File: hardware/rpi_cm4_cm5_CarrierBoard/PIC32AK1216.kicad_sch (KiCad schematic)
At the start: 96 parts, among them J10 PR20206VBNN, Q21 2N7002, Q25 2N7002, Q26 2N7002, U1 PIC32AK1216GC41064-I/M7, U20 STWD100NYWY3F, Y3 20MHz

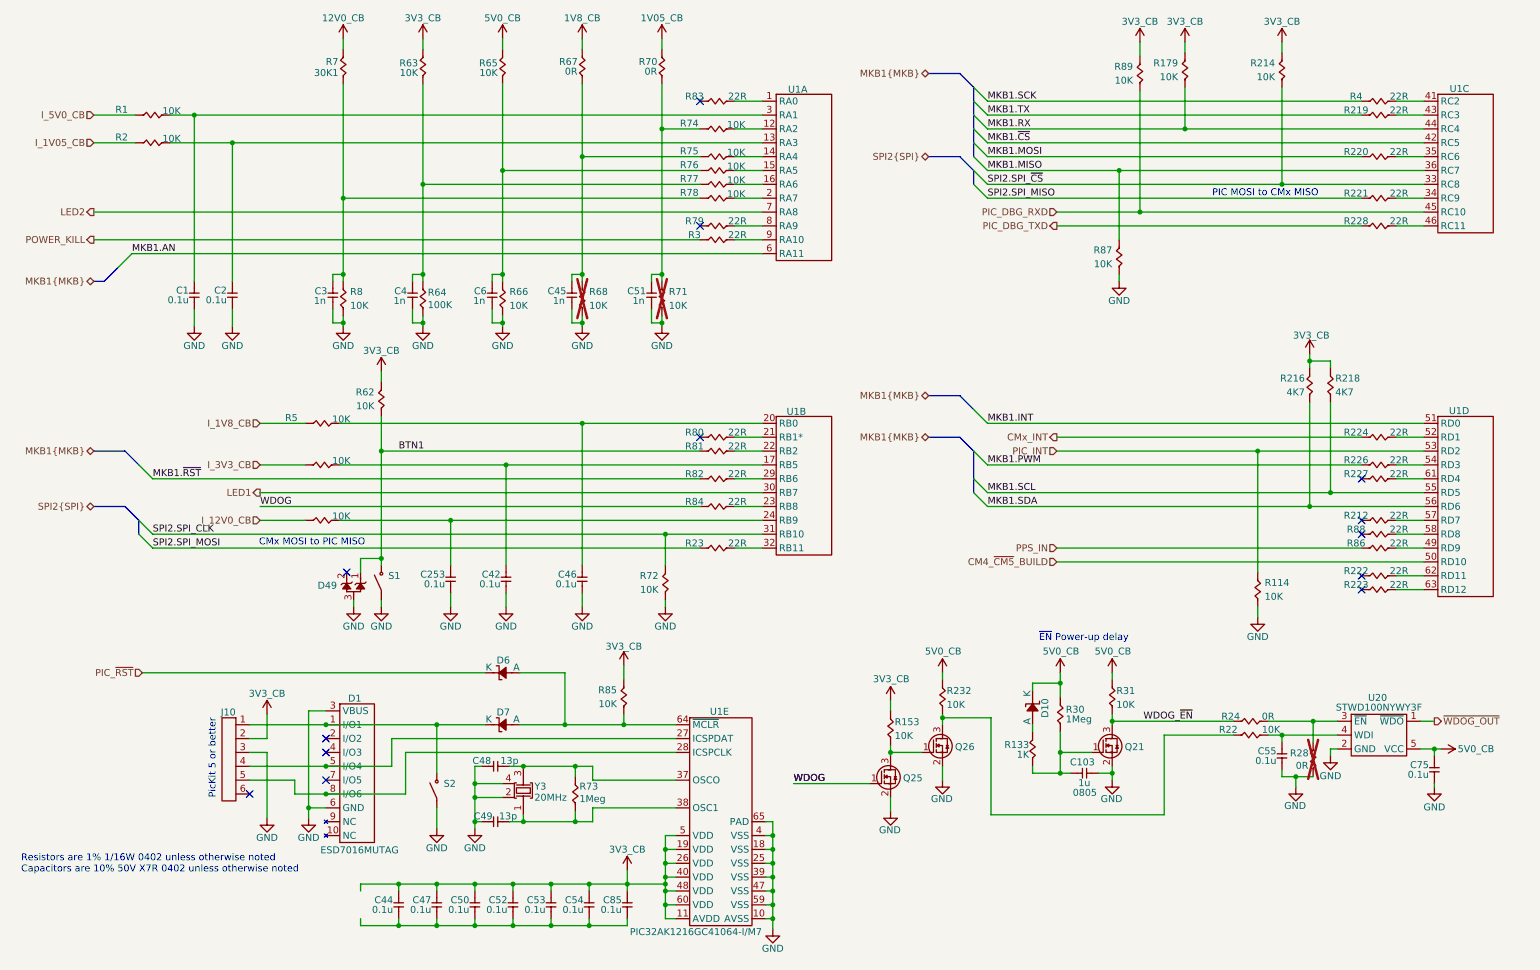
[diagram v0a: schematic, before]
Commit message: Cosmetic adjustments to schematics
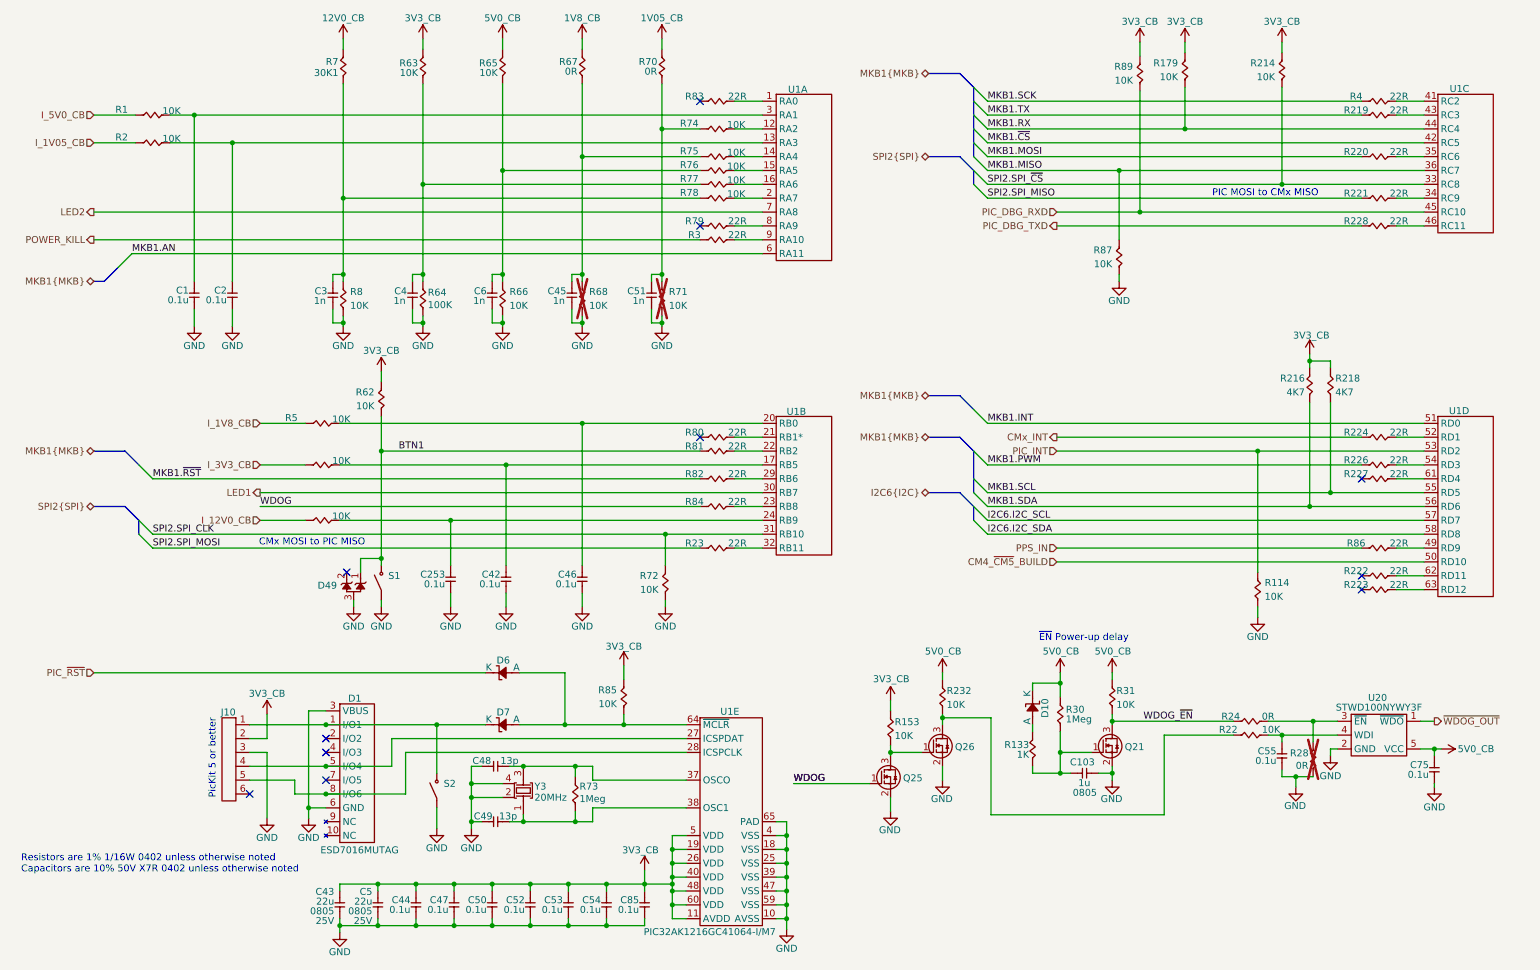
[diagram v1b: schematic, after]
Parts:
- removed R212, R88: 22R, footprint:RES_0402, symbol KicadCompDb:Resistors/RES_SMT_00015
- added C43, C5: 22u, footprint:CAP_NONPOL_0805, symbol KicadCompDb:Capacitors/CAP_CER_SMT_00011
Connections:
- net 3V3_CB: now also C43.2, C5.2
- net GND: now also C44.1, C47.1, C50.1, C52.1, C53.1, C54.1, C85.1, C43.1, C5.1
- net I2C6.I2C_SCL: now reaches U1.57 (RD7)
- net I2C6.I2C_SDA: now reaches U1.58 (RD8)
- no-connect marks 13 -> 11
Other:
- moved on the sheet: C44, C47, C50, C52, C53, C54, C85, U1E

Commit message: Significant update in PCB layout; Completed preliminary high speed rules definition and fanout of differential pairs + GND vias. Started routing high speed signals Slight changes to Pinout based on component placement
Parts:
- removed R83: 22R, footprint:RES_0402, symbol KicadCompDb:Resistors/RES_SMT_00015
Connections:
- net LED2: now also U1.1 (RA0); no longer U1.7 (RA8)
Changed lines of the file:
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@@
 	)
 	(no_connect
-		(at 137.16 31.115)
-	)
-	(no_connect
 		(at 137.16 92.71)
 	)
@@
 		(at 137.16 53.975)
 	)
+	(no_connect
+		(at 148.59 51.435)
+	)
 	(bus_entry
 		(at 187.325 28.575)
@@
 	(wire
 		(pts
+			(xy 26.035 31.115) (xy 148.59 31.115)
+		)
+		(stroke
+			(width 0)
+			(type default)
+		)
+	)
+	(wire
+		(pts
 			(xy 198.12 154.305) (xy 203.2 154.305)
 		)
@@
 	(wire
 		(pts
-			(xy 26.035 51.435) (xy 148.59 51.435)
-		)
-		(stroke
-			(width 0)
-			(type default)
-		)
-	)
-	(wire
-		(pts
 			(xy 78.105 180.975) (xy 78.105 182.245)
 		)
@@
 	(wire
 		(pts
-			(xy 143.51 31.115) (xy 148.59 31.115)
-		)
-		(stroke
-			(width 0)
-			(type default)
-		)
-	)
-	(wire
-		(pts
 			(xy 51.435 38.735) (xy 148.59 38.735)
 		)
@@
 		)
 	)
+	(hierarchical_label "LED2"
+		(shape output)
+		(at 26.035 31.115 180)
+		(effects
+			(font
+				(size 1.27 1.27)
+			)
+			(justify right)
+		)
+	)
 	(hierarchical_label "~{WDOG_OUT}"
 		(shape output)
@@
 		)
 	)
-	(hierarchical_label "LED2"
-		(shape output)
-		(at 26.035 51.435 180)
-		(effects
-			(font
-				(size 1.27 1.27)
-			)
-			(justify right)
-		)
-	)
 	(hierarchical_label "I2C6{I2C}"
 		(shape bidirectional)
@@
 					(unit 1)
 				)
-			)
-		)
-	)
-	(symbol
-		(lib_id "KicadCompDb:Resistors/RES_SMT_00015")
-		(at 142.24 31.115 180)
-		(unit 1)
-		(exclude_from_sim no)
-		(in_bom yes)
-		(on_board yes)
-		(dnp no)
-		(property "Reference" "R83"
-			(at 136.144 30.226 0)
-			(effects
-				(font
-					(size 1.27 1.27)
-				)
-			)
-		)
-		(property "Value" "22R"
-			(at 144.018 30.226 0)
-			(effects
-				(font
-					(size 1.27 1.27)
-				)
-			)
-		)
-		(property "Footprint" "footprint:RES_0402"
-			(at 141.732 9.017 0)
-			(effects
-				(font
-					(size 1.27 1.27)
-				)
-				(hide yes)
-			)
-		)
-		(property "Datasheet" "https://www.yageogroup.com/content/datasheet/asset/file/PYU-RC_GROUP_51_ROHS_L"
-			(at 142.24 31.115 0)
-			(effects
-				(font
-					(size 1.27 1.27)
-				)
-				(hide yes)
-			)
-		)
-		(property "Description" "RES 22 OHM 1% 1/16W 0402"
-			(at 140.462 21.209 0)
-			(effects
-				(font
-					(size 1.27 1.27)
-				)
-				(hide yes)
-			)
-		)
-		(property "Tolerance" "1%"
-			(at 141.986 10.795 0)
-			(effects
-				(font
-					(size 1.27 1.27)
-				)
-				(hide yes)
-			)
-		)
-		(property "Power" "1/16W"
-			(at 141.986 16.891 0)
-			(effects
-				(font
-					(size 1.27 1.27)
-				)
-				(hide yes)
-			)
-		)
-		(property "Package" "0402"
-			(at 142.24 14.859 0)
-			(effects
-				(font
-					(size 1.27 1.27)
-				)
-				(hide yes)
-			)
-		)
-		(property "Manufacturer" "YAGEO"
-			(at 141.986 12.827 0)
-			(effects
-				(font
-					(size 1.27 1.27)
-				)
-				(hide yes)
-			)
-		)
-		(property "Manufacturer Part Number" "RC0402FR-0722RL"
-			(at 141.986 23.241 0)
-			(effects
-				(font
-					(size 1.27 1.27)
-				)
-				(hide yes)
-			)
-		)
-		(property "Distributor" "DigiKey"
-			(at 142.24 25.273 0)
-			(effects
-				(font
-					(size 1.27 1.27)
-				)
-				(hide yes)
-			)
-		)
-		(property "Distributor Part Number" "311-22.0LRCT-ND"
-			(at 141.478 18.923 0)
-			(effects
-				(font
-					(size 1.27 1.27)
-				)
-				(hide yes)
-			)
-		)
-		(property "Temperature Coefficient" "±100ppm/°C"
-			(at 142.24 31.115 0)
-			(effects
-				(font
-					(size 1.27 1.27)
-				)
-				(hide yes)
-			)
-		)
-		(property "Operating Temperature" "-55°C ~ 155°C"
-			(at 141.478 6.731 0)
-			(effects
-				(font
-					(size 1.27 1.27)
-				)
-				(hide yes)
-			)
-		)
-		(property "Type" "RES SMT"
-			(at 142.24 31.115 0)
-			(show_name yes)
-			(effects
-				(font
-					(size 1.27 1.27)
-				)
-				(hide yes)
-			)
-		)
-		(property "Dimensions" "1.00mm x 0.50mm"
-			(at 142.24 31.115 0)
-			(show_name yes)
-			(effects
-				(font
-					(size 1.27 1.27)
-				)
-				(hide yes)
-			)
-		)
-		(pin "1"
-		)
-		(pin "2"
-		)
-		(instances
-			(project "rpi_cm4_cm5_CarrierBoard"
-				(path "/7dcdf741-90ca-4333-848c-806f4d64158e/7cb911d0-d4f5-46a6-8f4b-d261141d8579"
-					(reference "R83")
-					(unit 1)
-				)

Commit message: Continue working on the layout. Completed most of power planes planning and pouring Completed all DiffPairs routing and length matching (preliminary)
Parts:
- removed C2: 0.1u, footprint:CAP_NONPOL_0402, symbol KicadCompDb:Capacitors/CAP_CER_SMT_00001
- removed R2: 10K, footprint:RES_0402, symbol KicadCompDb:Resistors/RES_SMT_00013
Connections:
- no-connect marks 11 -> 12

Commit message: Significant update Stackup changed from 6 to 8 layers Changed design notes accordingly Re-routed all differential pairs and length match / skew match Fanout critical signals away from dense areas 95% routing completed
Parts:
- removed R224: 22R, footprint:RES_0402, symbol KicadCompDb:Resistors/RES_SMT_00015
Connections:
- net CM4_~{CM5}_BUILD: now also U1.52 (RD1); no longer U1.50 (RD10)
- net CMx_INT: now also U1.50 (RD10)
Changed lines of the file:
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@@
 	(title_block
 		(title "RPI CMx Carrier")
-		(date "2026-01-22")
+		(date "2026-02-13")
 		(rev "2.00-0A")
 		(comment 1 "Jean-Francois Bilodeau")
@@
 	(wire
 		(pts
-			(xy 202.565 92.71) (xy 258.445 92.71)
-		)
-		(stroke
-			(width 0)
-			(type default)
-		)
-	)
-	(wire
-		(pts
-			(xy 264.795 92.71) (xy 269.875 92.71)
+			(xy 202.565 92.71) (xy 269.875 92.71)
 		)
 		(stroke
@@
 		)
 	)
+	(hierarchical_label "CMx_INT"
+		(shape output)
+		(at 202.565 115.57 180)
+		(effects
+			(font
+				(size 1.27 1.27)
+			)
+			(justify right)
+		)
+	)
 	(hierarchical_label "PPS_IN"
 		(shape input)
@@
 		)
 	)
-	(hierarchical_label "CMx_INT"
-		(shape output)
+	(hierarchical_label "CM4_~{CM5}_BUILD"
+		(shape input)
 		(at 202.565 92.71 180)
 		(effects
@@
 		)
 	)
-	(hierarchical_label "CM4_~{CM5}_BUILD"
-		(shape input)
-		(at 202.565 115.57 180)
-		(effects
-			(font
-				(size 1.27 1.27)
-			)
-			(justify right)
-		)
-	)
 	(hierarchical_label "PIC_~{RST}"
 		(shape input)
@@
 					(unit 1)
 				)
-			)
-		)
-	)
-	(symbol
-		(lib_id "KicadCompDb:Resistors/RES_SMT_00015")
-		(at 263.525 92.71 180)
-		(unit 1)
-		(exclude_from_sim no)
-		(in_bom yes)
-		(on_board yes)
-		(dnp no)
-		(property "Reference" "R224"
-			(at 257.429 91.821 0)
-			(effects
-				(font
-					(size 1.27 1.27)
-				)
-			)
-		)
-		(property "Value" "22R"
-			(at 265.303 91.821 0)
-			(effects
-				(font
-					(size 1.27 1.27)
-				)
-			)
-		)
-		(property "Footprint" "footprint:RES_0402"
-			(at 263.017 70.612 0)
-			(effects
-				(font
-					(size 1.27 1.27)
-				)
-				(hide yes)
-			)
-		)
-		(property "Datasheet" "https://www.yageogroup.com/content/datasheet/asset/file/PYU-RC_GROUP_51_ROHS_L"
-			(at 263.525 92.71 0)
-			(effects
-				(font
-					(size 1.27 1.27)
-				)
-				(hide yes)
-			)
-		)
-		(property "Description" "RES 22 OHM 1% 1/16W 0402"
-			(at 261.747 82.804 0)
-			(effects
-				(font
-					(size 1.27 1.27)
-				)
-				(hide yes)
-			)
-		)
-		(property "Tolerance" "1%"
-			(at 263.271 72.39 0)
-			(effects
-				(font
-					(size 1.27 1.27)
-				)
-				(hide yes)
-			)
-		)
-		(property "Power" "1/16W"
-			(at 263.271 78.486 0)
-			(effects
-				(font
-					(size 1.27 1.27)
-				)
-				(hide yes)
-			)
-		)
-		(property "Package" "0402"
-			(at 263.525 76.454 0)
-			(effects
-				(font
-					(size 1.27 1.27)
-				)
-				(hide yes)
-			)
-		)
-		(property "Manufacturer" "YAGEO"
-			(at 263.271 74.422 0)
-			(effects
-				(font
-					(size 1.27 1.27)
-				)
-				(hide yes)
-			)
-		)
-		(property "Manufacturer Part Number" "RC0402FR-0722RL"
-			(at 263.271 84.836 0)
-			(effects
-				(font
-					(size 1.27 1.27)
-				)
-				(hide yes)
-			)
-		)
-		(property "Distributor" "DigiKey"
-			(at 263.525 86.868 0)
-			(effects
-				(font
-					(size 1.27 1.27)
-				)
-				(hide yes)
-			)
-		)
-		(property "Distributor Part Number" "311-22.0LRCT-ND"
-			(at 262.763 80.518 0)
-			(effects
-				(font
-					(size 1.27 1.27)
-				)
-				(hide yes)
-			)
-		)
-		(property "Temperature Coefficient" "±100ppm/°C"
-			(at 263.525 92.71 0)
-			(effects
-				(font
-					(size 1.27 1.27)
-				)
-				(hide yes)
-			)
-		)
-		(property "Operating Temperature" "-55°C ~ 155°C"
-			(at 262.763 68.326 0)
-			(effects
-				(font
-					(size 1.27 1.27)
-				)
-				(hide yes)
-			)
-		)
-		(property "Type" "RES SMT"
-			(at 263.525 92.71 0)
-			(show_name yes)
-			(effects
-				(font
-					(size 1.27 1.27)
-				)
-				(hide yes)
-			)
-		)
-		(property "Dimensions" "1.00mm x 0.50mm"
-			(at 263.525 92.71 0)
-			(show_name yes)
-			(effects
-				(font
-					(size 1.27 1.27)
-				)
-				(hide yes)
-			)
-		)
-		(pin "1"
-		)
-		(pin "2"
-		)
-		(instances
-			(project "rpi_cm4_cm5_CarrierBoard"
-				(path "/7dcdf741-90ca-4333-848c-806f4d64158e/7cb911d0-d4f5-46a6-8f4b-d261141d8579"
-					(reference "R224")
-					(unit 1)
-				)
